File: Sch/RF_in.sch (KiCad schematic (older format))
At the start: 10 parts

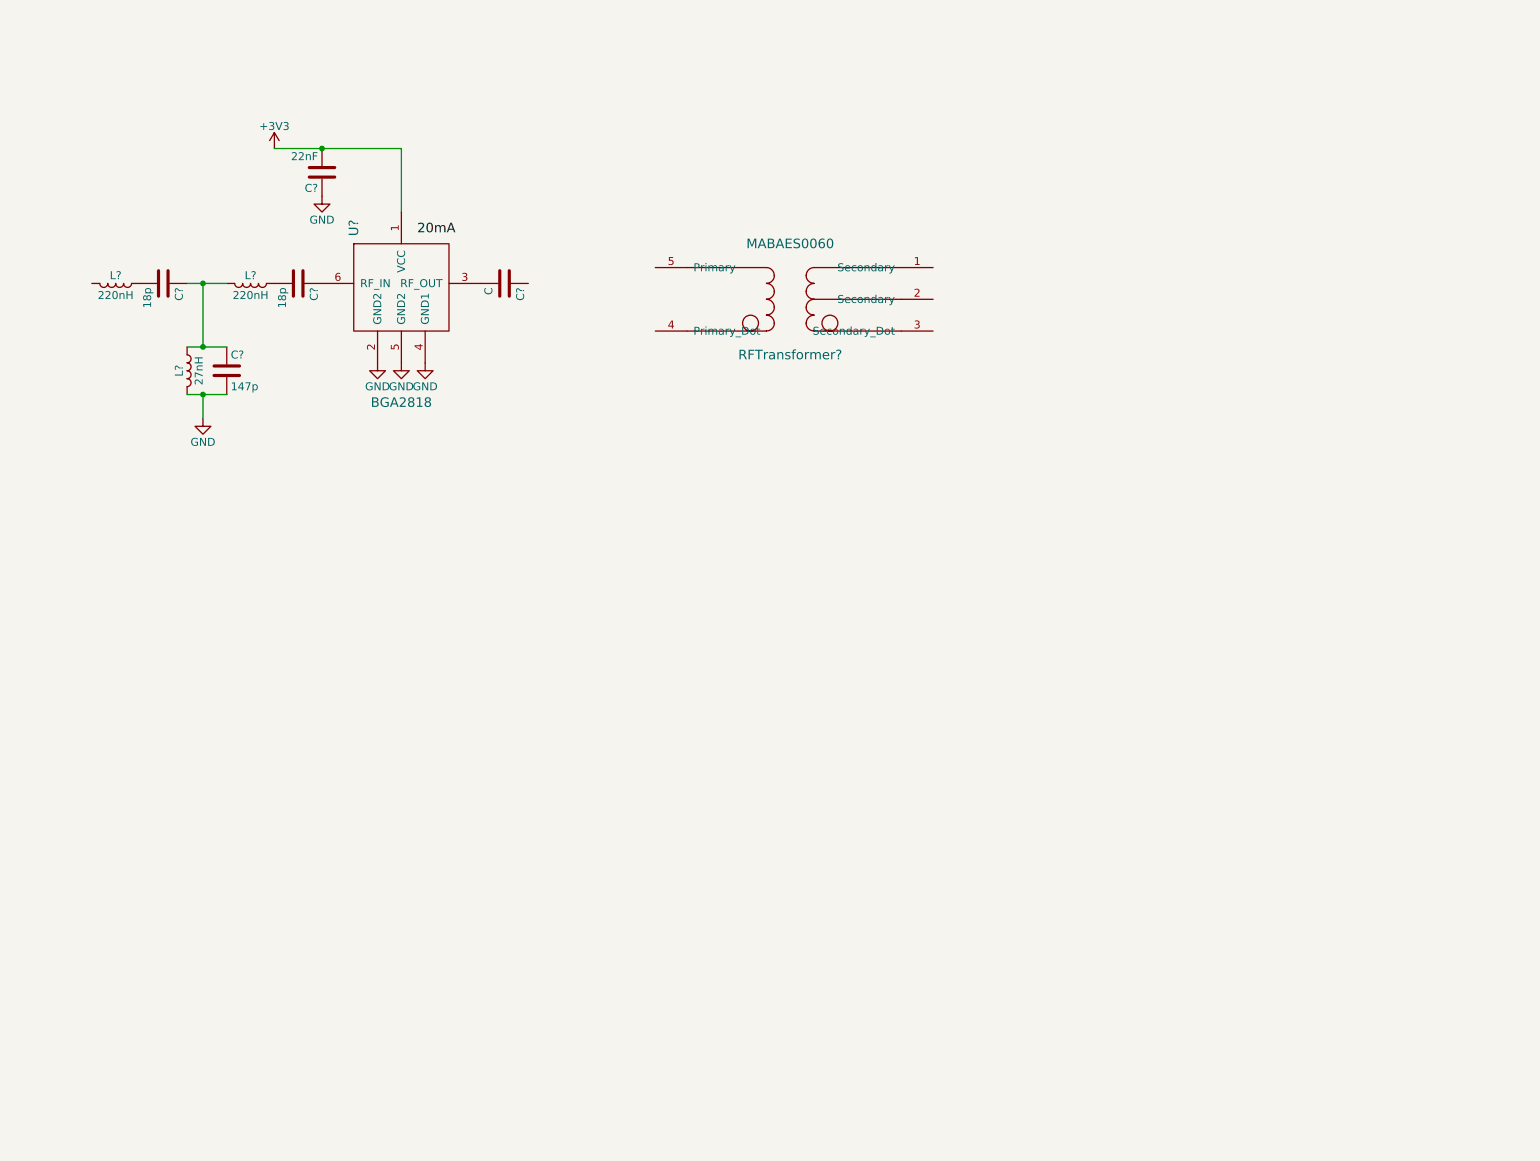
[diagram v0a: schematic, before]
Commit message: Add ADC, CN1/CN2
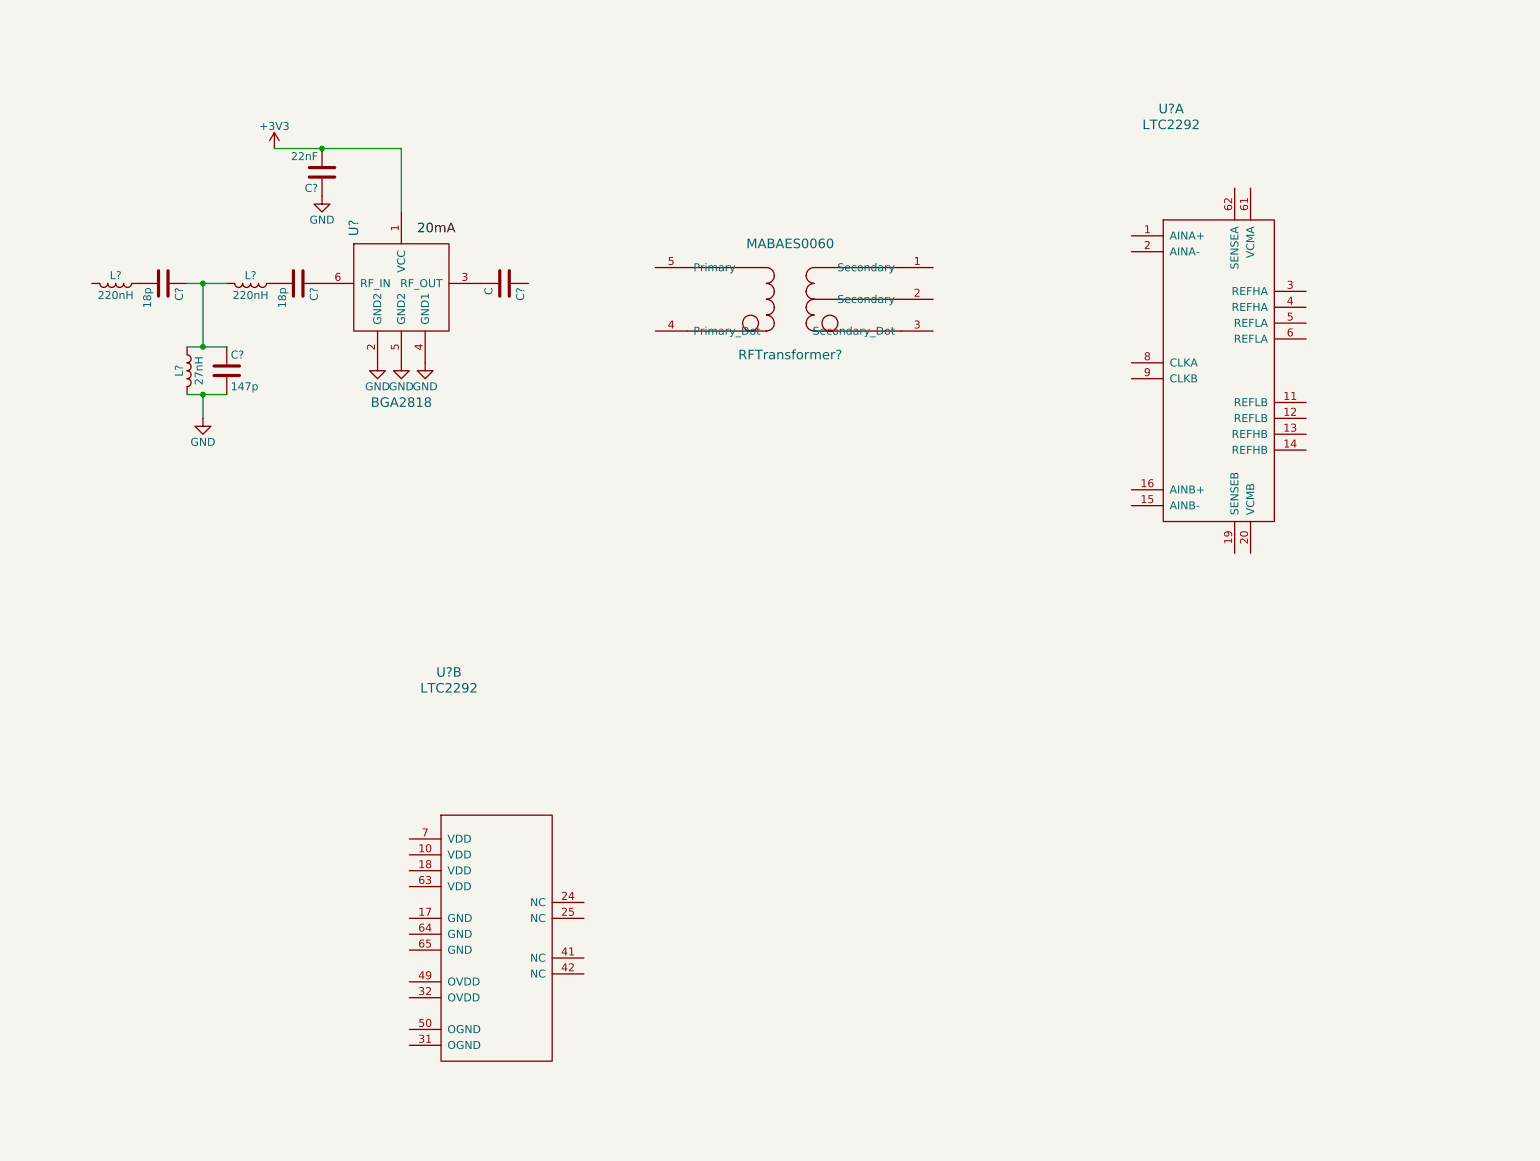
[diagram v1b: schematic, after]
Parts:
- added U? (x2): LTC2292, symbol LTC2292
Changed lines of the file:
@@
+	1    0    0    -1
+$EndComp
+$Comp
+L LTC2292 U?
+U 1 1 58A30835
+P 8600 2750
+F 0 "U?" H 8300 4400 60  0000 C CNN
+F 1 "LTC2292" H 8300 4300 60  0000 C CNN
+F 2 "" H 8600 2750 60  0001 C CNN
+F 3 "" H 8600 2750 60  0001 C CNN
+	1    8600 2750
+	1    0    0    -1
+$EndComp
+$Comp
+L LTC2292 U?
+U 2 1 58A30943
+P 4050 6300
+F 0 "U?" H 3750 7950 60  0000 C CNN
+F 1 "LTC2292" H 3750 7850 60  0000 C CNN
+F 2 "" H 4050 6300 60  0001 C CNN
+F 3 "" H 4050 6300 60  0001 C CNN
+	2    4050 6300
 	1    0    0    -1
 $EndComp

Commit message: modify
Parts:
- gave numbers to parts that had none: 11
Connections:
- wire segments 7 -> 20
- no-connect marks 0 -> 4
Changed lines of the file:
@@
 $EndDescr
 $Comp
-L BGA2818 U?
+L BGA2818 U2
 U 1 1 58A1C106
 P 3450 2250
-F 0 "U?" V 3150 2650 60  0000 C CNN
+F 0 "U2" V 3150 2650 60  0000 C CNN
 F 1 "BGA2818" H 3450 1550 60  0000 C CNN
 F 2 "" H 3450 2300 60  0001 C CNN
@@
 $EndComp
 $Comp
-L GND #PWR?
+L GND #PWR030
 U 1 1 58A1C19C
 P 3600 2700
-F 0 "#PWR?" H 3600 2450 50  0001 C CNN
+F 0 "#PWR030" H 3600 2450 50  0001 C CNN
 F 1 "GND" H 3600 2550 50  0000 C CNN
 F 2 "" H 3600 2700 50  0000 C CNN
@@
 $EndComp
 $Comp
-L GND #PWR?
+L GND #PWR031
 U 1 1 58A1C1B6
 P 3450 2700
-F 0 "#PWR?" H 3450 2450 50  0001 C CNN
+F 0 "#PWR031" H 3450 2450 50  0001 C CNN
 F 1 "GND" H 3450 2550 50  0000 C CNN
 F 2 "" H 3450 2700 50  0000 C CNN
@@
 $EndComp
 $Comp
-L GND #PWR?
+L GND #PWR032
 U 1 1 58A1C1C7
 P 3300 2700
-F 0 "#PWR?" H 3300 2450 50  0001 C CNN
+F 0 "#PWR032" H 3300 2450 50  0001 C CNN
 F 1 "GND" H 3300 2550 50  0000 C CNN
 F 2 "" H 3300 2700 50  0000 C CNN
@@
 $EndComp
 $Comp
-L C C?
+L C C26
 U 1 1 58A1C69B
 P 4100 2200
-F 0 "C?" H 4125 2300 50  0000 L CNN
+F 0 "C26" H 4125 2300 50  0000 L CNN
 F 1 "C" H 4125 2100 50  0000 L CNN
 F 2 "" H 4138 2050 50  0000 C CNN
@@
 $EndComp
 $Comp
-L GND #PWR?
+L GND #PWR033
 U 1 1 58A1C6CA
 P 2950 1650
-F 0 "#PWR?" H 2950 1400 50  0001 C CNN
+F 0 "#PWR033" H 2950 1400 50  0001 C CNN
 F 1 "GND" H 2950 1500 50  0000 C CNN
 F 2 "" H 2950 1650 50  0000 C CNN
@@
 $EndComp
 $Comp
-L +3V3 #PWR?
+L +3V3 #PWR034
 U 1 1 58A1C6DD
 P 2650 1350
-F 0 "#PWR?" H 2650 1200 50  0001 C CNN
+F 0 "#PWR034" H 2650 1200 50  0001 C CNN
 F 1 "+3V3" H 2650 1490 50  0000 C CNN
 F 2 "" H 2650 1350 50  0000 C CNN
@@
 $EndComp
 $Comp
-L C C?
+L C C25
 U 1 1 58A1C6F8
 P 2950 1500
-F 0 "C?" H 2975 1600 50  0000 L CNN
+F 0 "C25" H 2975 1600 50  0000 L CNN
 F 1 "22nF" H 2975 1400 50  0000 L CNN
 F 2 "" H 2988 1350 50  0000 C CNN
@@
 Connection ~ 2950 1350
 $Comp
-L L L?
+L L L2
 U 1 1 58A1CAF3
 P 1650 2200
-F 0 "L?" V 1600 2200 50  0000 C CNN
+F 0 "L2" V 1600 2200 50  0000 C CNN
 F 1 "220nH" V 1725 2200 50  0000 C CNN
 F 2 "" H 1650 2200 50  0000 C CNN
@@
 $EndComp
 $Comp
-L C C?
+L C C22
 U 1 1 58A1CB2F
 P 1950 2200
-F 0 "C?" H 1975 2300 50  0000 L CNN
+F 0 "C22" H 1975 2300 50  0000 L CNN
 F 1 "18p" H 1975 2100 50  0000 L CNN
 F 2 "" H 1988 2050 50  0000 C CNN
@@
 $EndComp
 $Comp
-L L L?
+L L L4
 U 1 1 58A1CBF1
 P 2500 2200
-F 0 "L?" V 2450 2200 50  0000 C CNN
+F 0 "L4" V 2450 2200 50  0000 C CNN
 F 1 "220nH" V 2575 2200 50  0000 C CNN
 F 2 "" H 2500 2200 50  0000 C CNN
@@
 $EndComp
 $Comp
-L C C?
+L C C24
 U 1 1 58A1CBF7
 P 2800 2200
-F 0 "C?" H 2825 2300 50  0000 L CNN
+F 0 "C24" H 2825 2300 50  0000 L CNN
 F 1 "18p" H 2825 2100 50  0000 L CNN
 F 2 "" H 2838 2050 50  0000 C CNN
@@
 	2100 2200 2350 2200
 $Comp
-L L L?
+L L L3
 U 1 1 58A1CC88
 P 2100 2750
-F 0 "L?" V 2050 2750 50  0000 C CNN
+F 0 "L3" V 2050 2750 50  0000 C CNN
 F 1 "27nH" V 2175 2750 50  0000 C CNN
 F 2 "" H 2100 2750 50  0000 C CNN
@@
 $EndComp
 $Comp
-L C C?
+L C C23
 U 1 1 58A1CC8E
 P 2350 2750
-F 0 "C?" H 2375 2850 50  0000 L CNN
+F 0 "C23" H 2375 2850 50  0000 L CNN
 F 1 "147p" H 2375 2650 50  0000 L CNN
 F 2 "" H 2388 2600 50  0000 C CNN
@@
 $EndComp
 $Comp
-L GND #PWR?
+L GND #PWR035
 U 1 1 58A1CD2C
 P 2200 3050
-F 0 "#PWR?" H 2200 2800 50  0001 C CNN
+F 0 "#PWR035" H 2200 2800 50  0001 C CNN
 F 1 "GND" H 2200 2900 50  0000 C CNN
 F 2 "" H 2200 3050 50  0000 C CNN
@@
 20mA
 $Comp
-L MABAES0060 RFTransformer?
+L MABAES0060 RFTransformer1
 U 1 1 58A1E2C2
 P 5900 2300
-F 0 "RFTransformer?" H 5900 1950 60  0000 C CNN
+F 0 "RFTransformer1" H 5900 1950 60  0000 C CNN
 F 1 "MABAES0060" H 5900 2650 60  0000 C CNN
 F 2 "" H 5950 2300 60  0001 C CNN
@@
 $EndComp
 $Comp
-L LTC2292 U?
-U 1 1 58A30835
+L LTC2292 U1
+U 2 1 58A30835
 P 8600 2750
-F 0 "U?" H 8300 4400 60  0000 C CNN
+F 0 "U1" H 8300 4400 60  0000 C CNN
 F 1 "LTC2292" H 8300 4300 60  0000 C CNN
 F 2 "" H 8600 2750 60  0001 C CNN
 F 3 "" H 8600 2750 60  0001 C CNN
-	1    8600 2750
-	1    0    0    -1
-$EndComp
-$Comp
-L LTC2292 U?
-U 2 1 58A30943
+	2    8600 2750
+	1    0    0    -1
+$EndComp
+$Comp
+L LTC2292 U1
+U 1 1 58A30943
 P 4050 6300
-F 0 "U?" H 3750 7950 60  0000 C CNN
+F 0 "U1" H 3750 7950 60  0000 C CNN
 F 1 "LTC2292" H 3750 7850 60  0000 C CNN
 F 2 "" H 4050 6300 60  0001 C CNN
 F 3 "" H 4050 6300 60  0001 C CNN
-	2    4050 6300
-	1    0    0    -1
-$EndComp
+	1    4050 6300
+	1    0    0    -1
+$EndComp
+$Comp
+L +3V3 #PWR036
+U 1 1 58A443A9
+P 7850 1850
+F 0 "#PWR036" H 7850 1700 50  0001 C CNN
+F 1 "+3V3" H 7850 1990 50  0000 C CNN
+F 2 "" H 7850 1850 50  0000 C CNN
+F 3 "" H 7850 1850 50  0000 C CNN
+	1    7850 1850
+	1    0    0    -1
+$EndComp
+Wire Wire Line
+	7850 1850 7850 3150
+Wire Wire Line
+	7850 2100 8050 2100
+Wire Wire Line
+	7850 2200 8050 2200
+Connection ~ 7850 2100
+Connection ~ 7850 2200
+Wire Wire Line
+	7850 2400 8050 2400
+Connection ~ 7850 2300
+$Comp
+L GND #PWR037
+U 1 1 58A44759
+P 7600 3800
+F 0 "#PWR037" H 7600 3550 50  0001 C CNN
+F 1 "GND" H 7600 3650 50  0000 C CNN
+F 2 "" H 7600 3800 50  0000 C CNN
+F 3 "" H 7600 3800 50  0000 C CNN
+	1    7600 3800
+	1    0    0    -1
+$EndComp
+Wire Wire Line
+	7850 3050 8050 3050
+Connection ~ 7850 2400
+Wire Wire Line
+	7850 3150 8050 3150
+Connection ~ 7850 3050
+Wire Wire Line
+	8050 2650 7600 2650
+Wire Wire Line
+	7600 2650 7600 3800
+Wire Wire Line
+	8050 2750 7600 2750
+Connection ~ 7600 2750
+Wire Wire Line
+	8050 2850 7600 2850
+Connection ~ 7600 2850
+Wire Wire Line
+	8050 3350 7600 3350
+Connection ~ 7600 3350
+Wire Wire Line
+	7600 3450 8050 3450
+NoConn ~ 9150 2550
+NoConn ~ 9150 2650
+NoConn ~ 9150 2900
+NoConn ~ 9150 3000
+Connection ~ 7600 3450
+Wire Wire Line
+	8050 2300 7850 2300
 $EndSCHEMATC

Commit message: update
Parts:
- added C29, C30, C37, C38: 0.1u, symbol C
- added C31, C32, C40: 2.2u, symbol C
- added C33, C34, C35, C36: 1u, symbol C
- added C39: 12p, symbol C
- added R15: 50, symbol R
- added R16: 51, symbol R
- added R17, R18, R19, R20: 24.9, symbol R
- C26: value C -> 0.1u
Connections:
- net labels added: VCMA
- wire segments 20 -> 52
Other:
- note added: "BPF 70-90MHz"
- note added: "MAX 95mA"
- note added: "RF Amp"
- moved on the sheet: C22, C23, C24, C25, C26, L2, L3, L4, RFTransformer1, U1A, U1B, U2

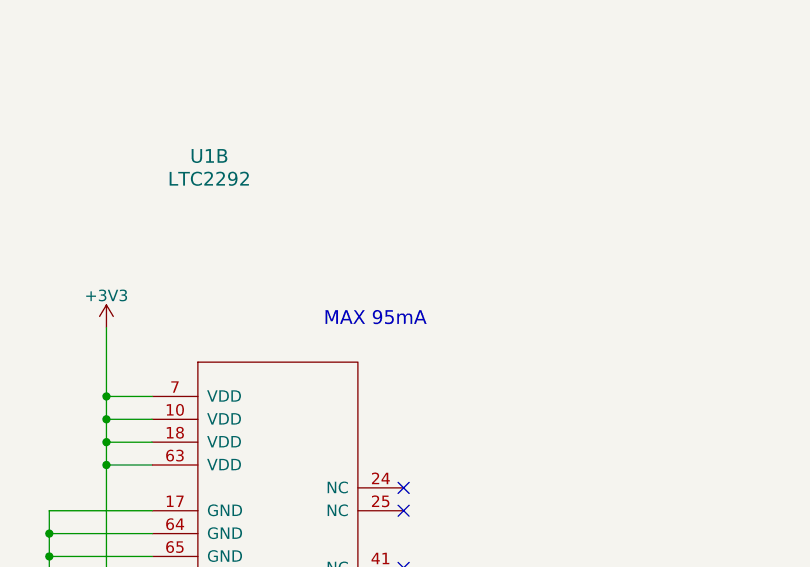
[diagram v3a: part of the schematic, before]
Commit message: Add 1.2V
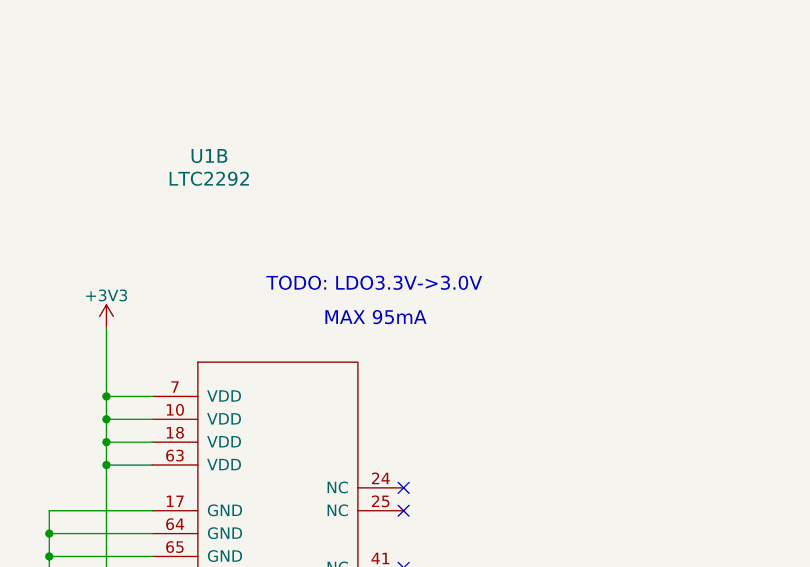
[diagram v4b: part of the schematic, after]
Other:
- note added: "TODO: LDO3.3V->3.0V"
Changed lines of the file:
@@
 $Descr A4 11693 8268
 encoding utf-8
-Sheet 5 6
+Sheet 5 7
 Title ""
 Date ""
@@
 Wire Wire Line
 	2000 7000 1550 7000
+Text Notes 2500 5350 0    60   ~ 0
+TODO: LDO3.3V->3.0V
 $EndSCHEMATC
